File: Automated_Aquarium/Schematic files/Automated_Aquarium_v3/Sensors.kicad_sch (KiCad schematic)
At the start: 3 parts

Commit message: init pcb
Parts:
- renumbered J_CON to J_CON1, J_DO to J_DO1, J_PH to J_PH1
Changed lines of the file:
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@@
   (symbol (lib_id "Connector_Generic:Conn_01x03") (at 111.76 76.2 0) (unit 1)
     (in_bom yes) (on_board yes) (dnp no) (fields_autoplaced)
-    (property "Reference" "J_PH" (at 114.3 75.565 0)
+    (property "Reference" "J_PH1" (at 114.3 75.565 0)
       (effects (font (size 1.27 1.27)) (justify left))
     )
@@
       (project "Automated_Aquarium_v3"
         (path "/953ef1f2-1b30-471f-8352-2e2b084ebc55/4e9bf6dc-f088-4e5f-8705-18ce454bedb2"
-          (reference "J_PH") (unit 1)
+          (reference "J_PH1") (unit 1)
         )
       )
@@
   (symbol (lib_id "Connector_Generic:Conn_01x03") (at 111.76 66.04 0) (unit 1)
     (in_bom yes) (on_board yes) (dnp no) (fields_autoplaced)
-    (property "Reference" "J_DO" (at 114.3 65.405 0)
+    (property "Reference" "J_DO1" (at 114.3 65.405 0)
       (effects (font (size 1.27 1.27)) (justify left))
     )
@@
       (project "Automated_Aquarium_v3"
         (path "/953ef1f2-1b30-471f-8352-2e2b084ebc55/4e9bf6dc-f088-4e5f-8705-18ce454bedb2"
-          (reference "J_DO") (unit 1)
+          (reference "J_DO1") (unit 1)
         )
       )
@@
   (symbol (lib_id "Connector_Generic:Conn_01x03") (at 111.76 86.36 0) (unit 1)
     (in_bom yes) (on_board yes) (dnp no) (fields_autoplaced)
-    (property "Reference" "J_CON" (at 114.3 85.725 0)
+    (property "Reference" "J_CON1" (at 114.3 85.725 0)
       (effects (font (size 1.27 1.27)) (justify left))
     )
@@
       (project "Automated_Aquarium_v3"
         (path "/953ef1f2-1b30-471f-8352-2e2b084ebc55/4e9bf6dc-f088-4e5f-8705-18ce454bedb2"
-          (reference "J_CON") (unit 1)
+          (reference "J_CON1") (unit 1)
         )
       )

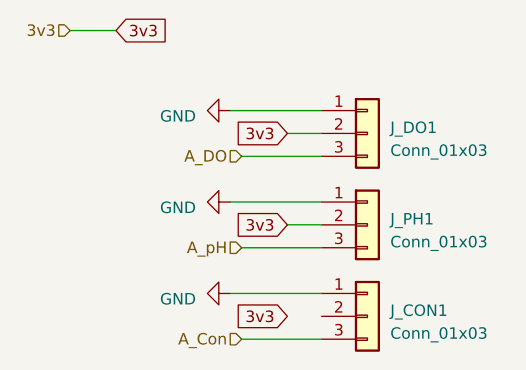
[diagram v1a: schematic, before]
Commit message: finish aqua schem, add inital layout
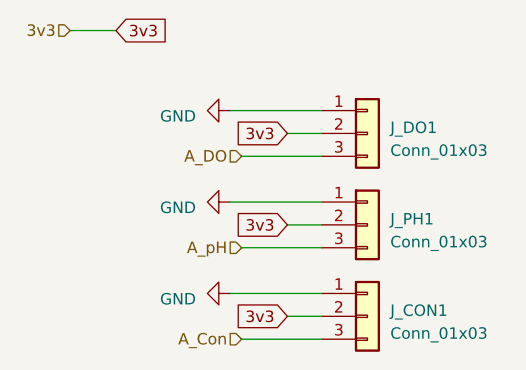
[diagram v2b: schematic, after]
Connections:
- net 3v3: now also J_CON1.2 (Pin_2)
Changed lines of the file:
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@@
+    (stroke (width 0) (type default))
+  )
+  (wire (pts (xy 102.87 86.36) (xy 106.68 86.36))
     (stroke (width 0) (type default))
   )
